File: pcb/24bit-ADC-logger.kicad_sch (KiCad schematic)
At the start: 21 parts, among them U1 REF5050AD, U2 ADS1232IPW, U3 TL071, U4 MAX15062A, U5 LP38693MP-5.0, U6 PicoW

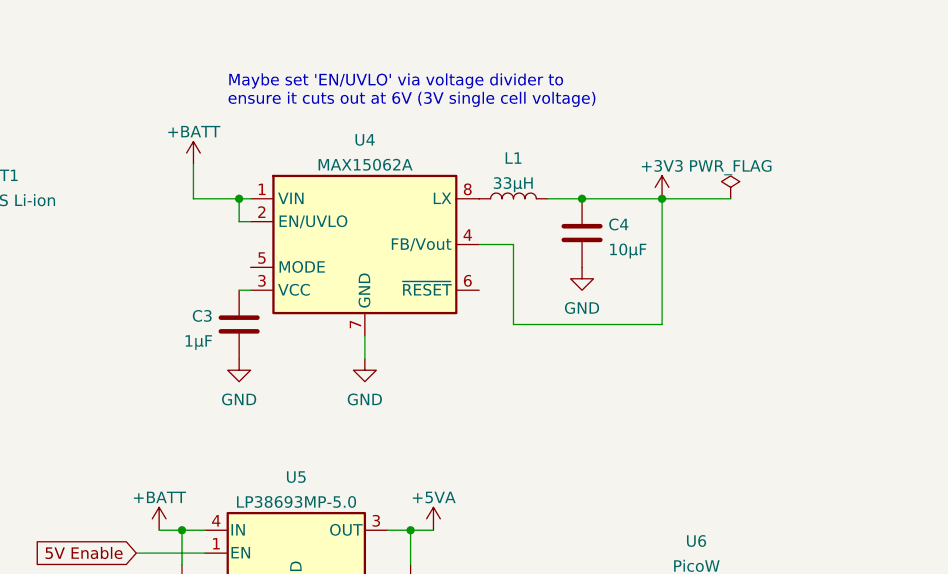
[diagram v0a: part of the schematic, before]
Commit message: feat: add 3.3V step-down regulator
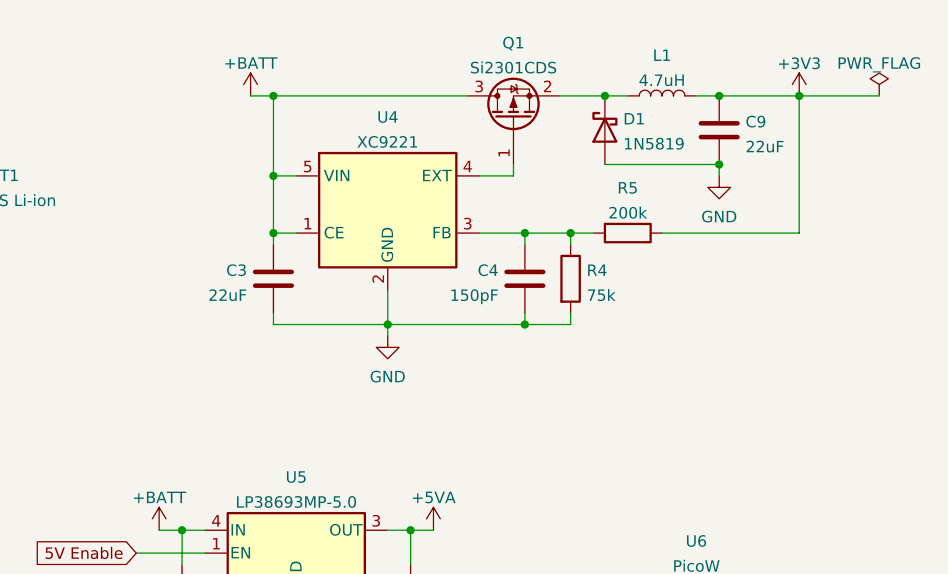
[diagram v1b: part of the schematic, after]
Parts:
- removed U4: MAX15062A, Package_DFN_QFN:DFN-8_2x2mm_P0.5mm, symbol Regulator_Switching:MAX15062A
- added C9: 22uF, symbol Device:C
- added D1: 1N5819, symbol Device:D_Schottky
- added Q1: Si2301CDS, Package_TO_SOT_SMD:SOT-23, symbol Si2301CDS:Si2301CDS
- added R4: 75k, symbol Device:R
- added R5: 200k, symbol Device:R
- added U4: XC9221, Package_TO_SOT_SMD:SOT-23-5, symbol XC9221:XC9221
- C3: value 1µF -> 22uF
- C4: value 10µF -> 150pF
- L1: value 33µH -> 4.7uH
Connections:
- net +3V3: now also C9.1, R5.1; no longer C4.1
- net +BATT: now also C3.1, Q1.3 (D), U4.1 (CE), U4.5 (VIN)
- net GND: now also C9.2, D1.2 (A), R4.2, U4.2 (GND)
- net at L1.1: now also D1.1 (K), Q1.2 (S)
- new net: Q1.1 (G), U4.4 (EXT)
- new net: C4.1, R4.1, R5.2, U4.3 (FB)
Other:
- note removed: "Maybe set 'EN/UVLO' via voltage divider to ensure it cuts out at 6V (3V single cell voltage)"
